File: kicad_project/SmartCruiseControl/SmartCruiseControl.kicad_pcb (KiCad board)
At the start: 2 copper layers, 100 x 100 mm, 45 parts, among them J1 Accelerator pedal, J2 CAN bus, J3 Brake + clutch, J4 Buttons + led, J5 USB 5V, K1 HK19F-DC 5V-SHG, Q1 IRLZ44N, Q2 2N3904, Q3 2N3904, Q4 2N3904, Q5 2N3904, U1 SN65HVD230, U2 ESP32DevKitv1

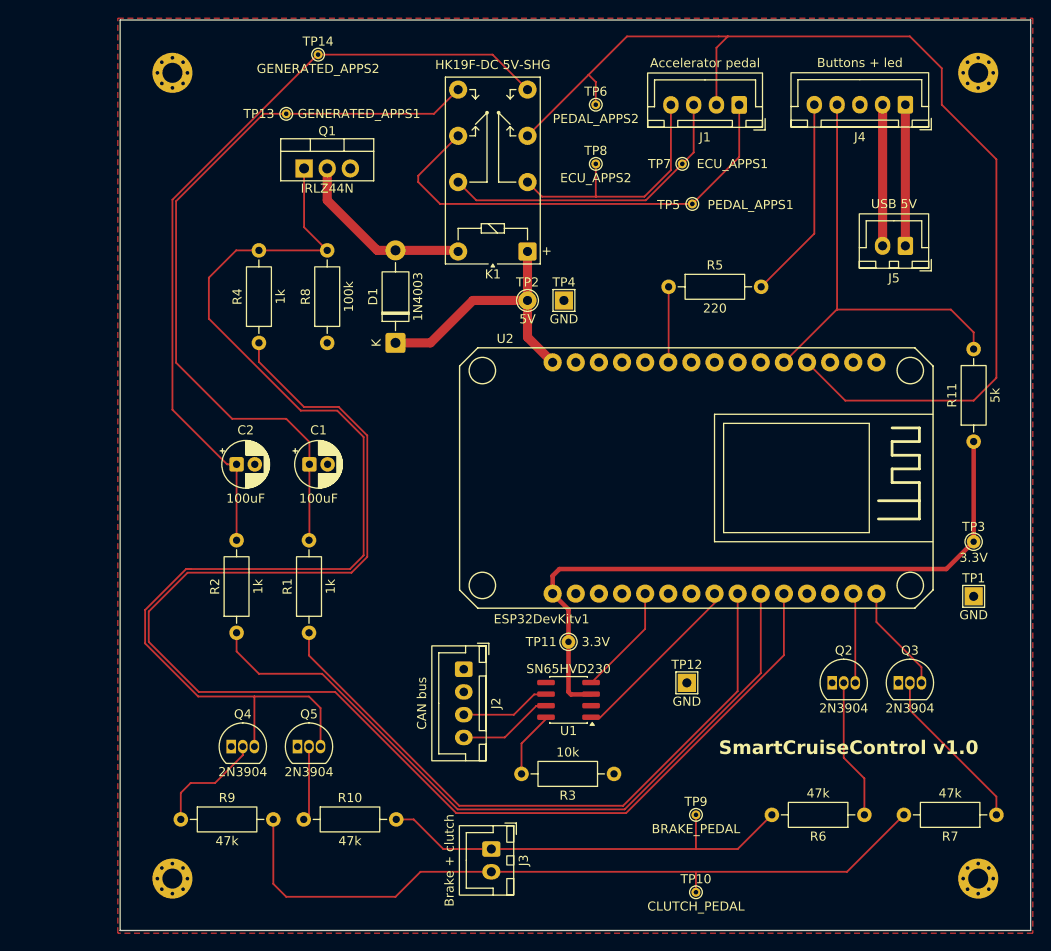
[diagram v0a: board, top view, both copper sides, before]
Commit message: Updated board to v1.1
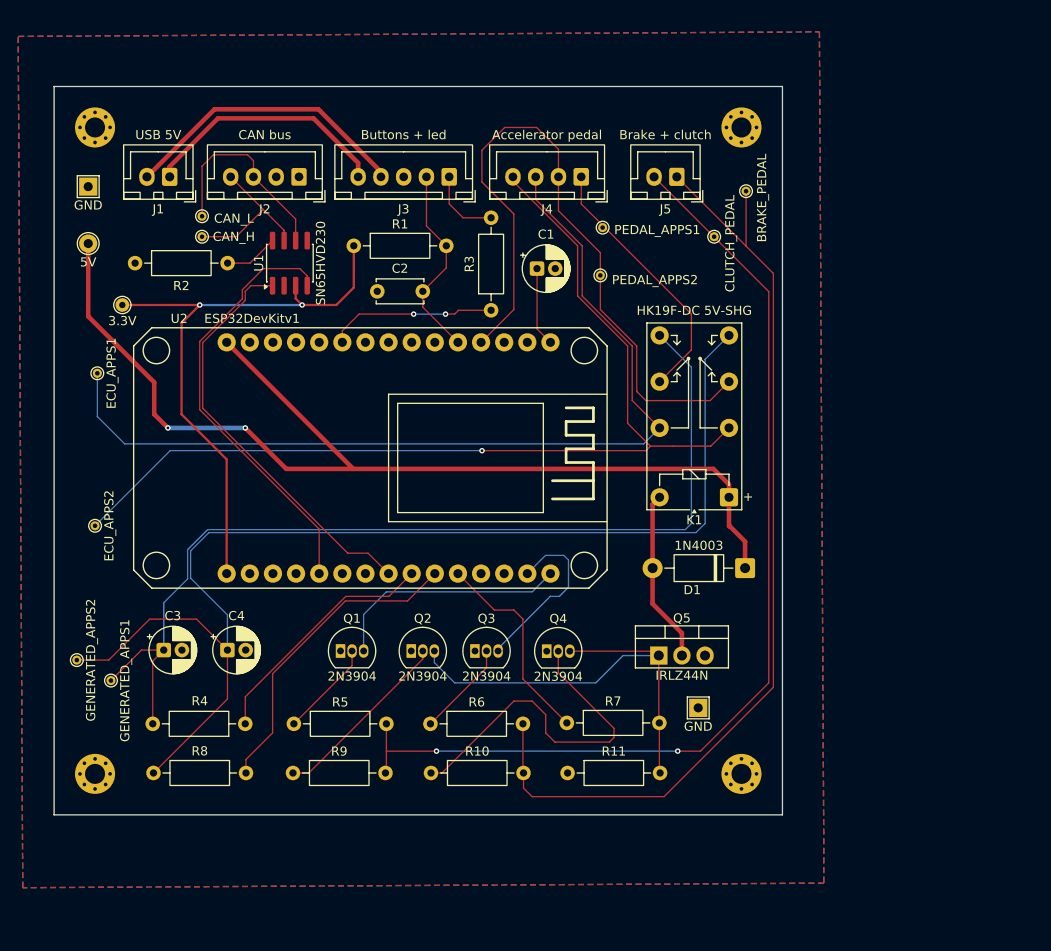
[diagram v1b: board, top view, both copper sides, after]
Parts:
- added C1: 1uF, Capacitor_THT:CP_Radial_D5.0mm_P2.00mm, F.Cu at (153.0, 70.0)
- added C2: 100nF, Capacitor_THT:C_Disc_D5.0mm_W2.5mm_P5.00mm, F.Cu at (140.5, 72.5)
- R1: renamed from R11; value 5k -> 5.1k
- R10, R6, R9: value 47k -> 100k
- R5: renamed from R7; value 47k -> 100k
- TP10: value CLUTCH_PEDAL -> ECU_APPS1
- TP11: value 3.3V -> ECU_APPS2; footprint TestPoint:TestPoint_THTPad_D1.5mm_Drill0.7mm -> TestPoint:TestPoint_THTPad_D1.0mm_Drill0.5mm
- TP12: value GND -> GENERATED_APPS2; footprint TestPoint:TestPoint_THTPad_2.0x2.0mm_Drill1.0mm -> TestPoint:TestPoint_THTPad_D1.0mm_Drill0.5mm
- TP14: value GENERATED_APPS2 -> GND; footprint TestPoint:TestPoint_THTPad_D1.0mm_Drill0.5mm -> TestPoint:TestPoint_THTPad_2.0x2.0mm_Drill1.0mm
- TP2: value 5V -> BRAKE_PEDAL; footprint TestPoint:TestPoint_THTPad_D2.0mm_Drill1.0mm -> TestPoint:TestPoint_THTPad_D1.0mm_Drill0.5mm
- TP3: value 3.3V -> CAN_L; footprint TestPoint:TestPoint_THTPad_D1.5mm_Drill0.7mm -> TestPoint:TestPoint_THTPad_D1.0mm_Drill0.5mm
- TP4: value GND -> PEDAL_APPS1; footprint TestPoint:TestPoint_THTPad_2.0x2.0mm_Drill1.0mm -> TestPoint:TestPoint_THTPad_D1.0mm_Drill0.5mm
- TP5: value PEDAL_APPS1 -> CAN_H
- TP6: value PEDAL_APPS2 -> CLUTCH_PEDAL
- TP7: value ECU_APPS1 -> 5V; footprint TestPoint:TestPoint_THTPad_D1.0mm_Drill0.5mm -> TestPoint:TestPoint_THTPad_D2.0mm_Drill1.0mm
- TP8: value ECU_APPS2 -> PEDAL_APPS2
- TP9: value BRAKE_PEDAL -> 3.3V; footprint TestPoint:TestPoint_THTPad_D1.0mm_Drill0.5mm -> TestPoint:TestPoint_THTPad_D1.5mm_Drill0.7mm
- moved H1 127.3 mm to (104.5, 54.5)
- moved TP1 107.2 mm to (103.8, 61.0)
- moved H2 103.5 mm to (175.5, 54.5)
- moved TP3 92.0 mm to (116.2, 64.2)
- moved TP10 87.0 mm to (104.8, 81.5), turned to 90 degrees
- moved TP9 84.3 mm to (107.5, 74.0)
- moved TP14 83.0 mm to (170.8, 118.2)
- moved H4 81.3 mm to (175.5, 125.5)
- moved J1 81.2 mm to (112.7, 59.9)
- moved R5 77.8 mm to (126.3, 120.0), turned to 0 degrees
- moved H3 77.5 mm to (104.5, 125.5)
- moved R2 76.9 mm to (108.9, 69.4), turned to 0 degrees
- moved J5 76.6 mm to (168.4, 59.9), turned to 180 degrees
- moved R1 71.4 mm to (132.9, 67.5), turned to 0 degrees
- moved TP12 67.0 mm to (102.5, 113.0), turned to 90 degrees
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- renumbered C1 to C3, C2 to C4, J5 to J1, J4 to J3, J1 to J4, J3 to J5, Q3 to Q1, Q4 to Q2, Q2 to Q3, Q5 to Q4, Q1 to Q5, R8 to R11, R3 to R2, R5 to R3, R1 to R4, R4 to R7, R2 to R8
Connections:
- net Net-(D1-A) renamed /RELAY_GND
- net Net-(Q3-C) renamed /CLUTCH_INPUT
- net Net-(U1-D) renamed /CAN_TTL_TX
- net Net-(U1-R) renamed /CAN_TTL_RX
- net Net-(U2-D18) renamed /PWM_GENERATED_APPS1
- net Net-(U2-D19) renamed /PWM_GENERATED_APPS2
- net Net-(U2-D21) renamed /RELAY_ENABLE
- J1 pad 1: +5V -> /5V_IN
- J1 pad 2: +5V -> /5V_OUT
- J3 pad 1: +5V -> /Net-(J2-Pin_1)
- J3 pad 2: +5V -> /BUTTON_KEY
- J3 pad 4: /BUTTON_KEY -> /5V_OUT
- J3 pad 5: Net-(J4-Pin_5) -> /5V_IN
- Q3 pad 3: Net-(Q2-C) (its old number) -> /BRAKE_INPUT
- R3 pad 2: Net-(J4-Pin_5) -> /Net-(J2-Pin_1)
- TP10 pad 1: /CLUTCH -> /ECU_APPS1
- TP11 pad 1: +3.3V -> /ECU_APPS2
- TP12 pad 1: GND -> /GENERATED_APPS2
- TP14 pad 1: /GENERATED_APPS2 -> GND
- TP2 pad 1: +5V -> /BRAKE
- TP3 pad 1: +3.3V -> /CAN_LOW
- TP4 pad 1: GND -> /PEDAL_APPS1
- TP5 pad 1: /PEDAL_APPS1 -> /CAN_HIGH
- TP6 pad 1: /PEDAL_APPS2 -> /CLUTCH
- TP7 pad 1: /ECU_APPS1 -> +5V
- TP8 pad 1: /ECU_APPS2 -> /PEDAL_APPS2
- TP9 pad 1: /BRAKE -> +3.3V
- U2 pad 14: Net-(Q2-C) (its old number) -> /BRAKE_INPUT
- U2 pad 16: unconnected-(U2-EN-Pad16) -> /EN
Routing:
- net /RELAY_ENABLE: track 152.0 -> 22.6 mm
- net /ECU_APPS2: track 28.4 -> 109.9 mm, vias 0 -> 1
- net Net-(Q2-C): track 127.3 -> 51.0 mm
- net /ECU_APPS1: track 34.1 -> 101.7 mm
- net /BRAKE: track 48.3 -> 106.4 mm
- net +5V: track 60.8 -> 117.7 mm, vias 0 -> 2
- net /PWM_GENERATED_APPS2: track 81.7 -> 34.5 mm
- net /PEDAL_APPS2: track 123.2 -> 76.0 mm
- net /PWM_GENERATED_APPS1: track 73.0 -> 26.8 mm
- net /GENERATED_APPS2: track 88.1 -> 128.7 mm
- net /CAN_TTL_RX: track 12.3 -> 48.0 mm
- net /5V_OUT: track 0.00 -> 32.2 mm
- net Net-(Q4-B): track 8.24 -> 38.6 mm
- net /CLUTCH: track 82.9 -> 111.3 mm, vias 0 -> 2
- net /5V_IN: track 0.00 -> 27.6 mm
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- added copper zone on B.Cu, net GND
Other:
- board size 100 x 100 mm -> 80 x 80 mm
- board text added: "SmartCruiseControl v1.1"
- board text removed: "SmartCruiseControl v1.0"
